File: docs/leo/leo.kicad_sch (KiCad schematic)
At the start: 21 parts, among them IC11 GAL16V8, IC20 74153, IC21 74LS273, IC29 74LS273, IC37 MB81C78A, IC38 MB81C78A, IC40 74LS04, IC41 GAL16V8, IC51 GAL16V8, IC52 74LS32, IC56 74LS245, IC57 74LS245, IC58 74LS244, IC59 74LS244, IC60 74LS244, IC61 74LS139, IC62 74LS20, IC8 7486

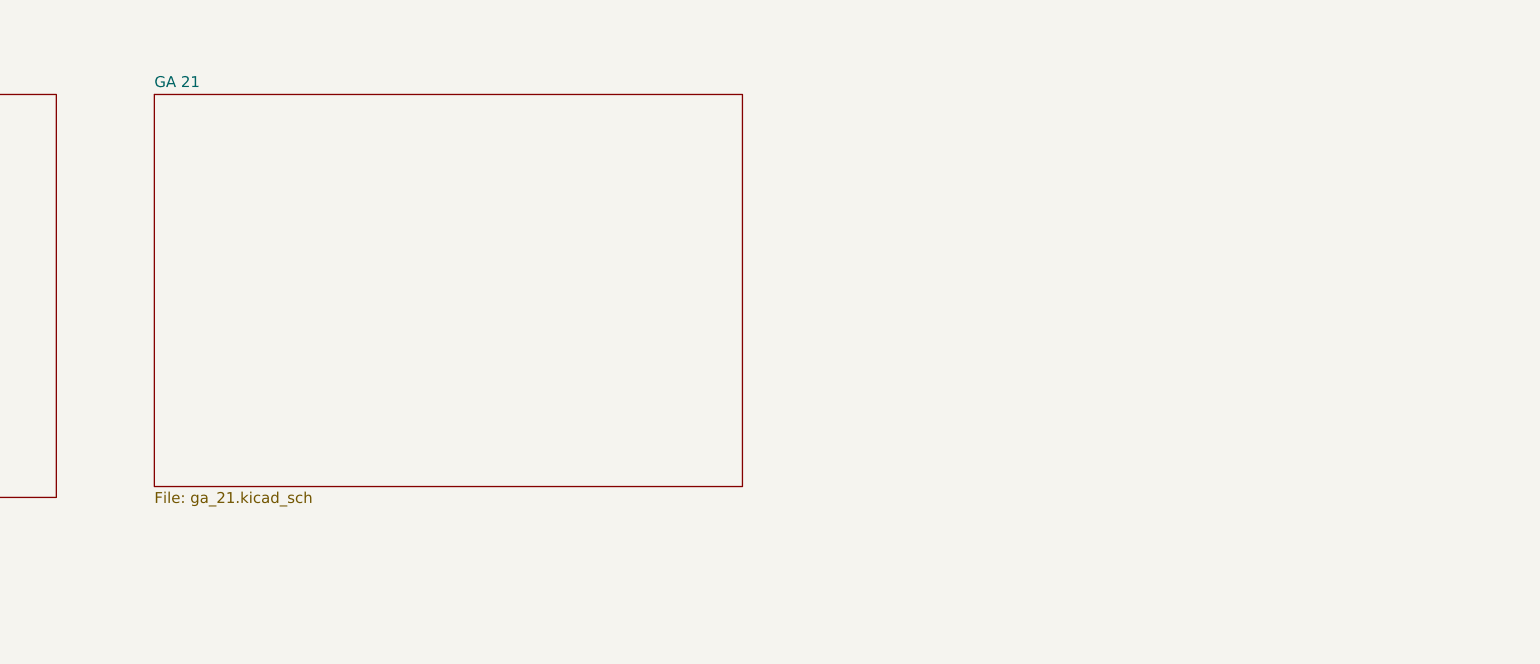
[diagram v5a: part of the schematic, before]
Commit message: Added GA22 symbol
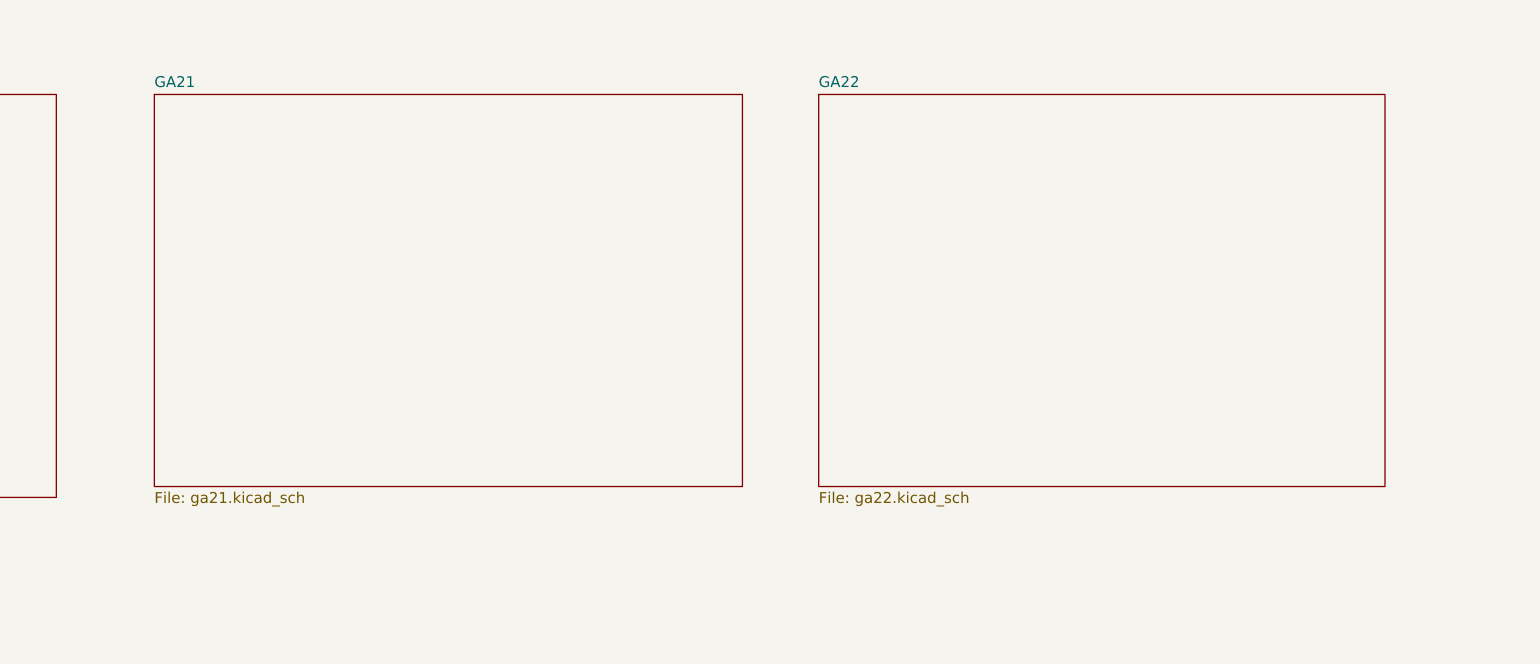
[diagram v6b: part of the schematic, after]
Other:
- sheet GA 21 renamed GA21
- added sheet GA22 (ga22.kicad_sch)
- sheet GA21: file ga_21.kicad_sch -> ga21.kicad_sch
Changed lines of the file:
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@@
     (stroke (width 0.1524) (type solid) (color 0 0 0 0))
     (fill (color 0 0 0 0.0000))
-    (property "Sheet name" "GA 21" (id 0) (at 285.75 41.1984 0)
-      (effects (font (size 1.27 1.27)) (justify left bottom))
-    )
-    (property "Sheet file" "ga_21.kicad_sch" (id 1) (at 285.75 88.2146 0)
+    (property "Sheet name" "GA21" (id 0) (at 285.75 41.1984 0)
+      (effects (font (size 1.27 1.27)) (justify left bottom))
+    )
+    (property "Sheet file" "ga21.kicad_sch" (id 1) (at 285.75 88.2146 0)
       (effects (font (size 1.27 1.27)) (justify left top))
     )
@@
     )
     (property "Sheet file" "palette_ram.kicad_sch" (id 1) (at 55.88 89.4846 0)
+      (effects (font (size 1.27 1.27)) (justify left top))
+    )
+  )
+  (sheet (at 363.22 41.91) (size 66.04 45.72) (fields_autoplaced)
+    (stroke (width 0.1524) (type solid) (color 0 0 0 0))
+    (fill (color 0 0 0 0.0000))
+    (property "Sheet name" "GA22" (id 0) (at 363.22 41.1984 0)
+      (effects (font (size 1.27 1.27)) (justify left bottom))
+    )
+    (property "Sheet file" "ga22.kicad_sch" (id 1) (at 363.22 88.2146 0)
       (effects (font (size 1.27 1.27)) (justify left top))
     )
@@
     (path "/3c8e9905-8b74-4eb3-9c18-3105ee09a33f" (page "4"))
     (path "/0bd61519-701e-4675-a889-b424ac477c32" (page "5"))
+    (path "/c1977d2d-8f37-45fb-befe-52187747618e" (page "6"))
   )
   (symbol_instances
@@
       (reference "IC62") (unit 2) (value "74LS20") (footprint "")
     )
+    (path "/c1977d2d-8f37-45fb-befe-52187747618e/7af1c0a0-2edc-4a0d-88a7-73759f63a8a1"
+      (reference "IC63") (unit 1) (value "GA22") (footprint "")
+    )
     (path "/3c8e9905-8b74-4eb3-9c18-3105ee09a33f/1a77a52a-b972-45fe-b376-224bbc5471ec"

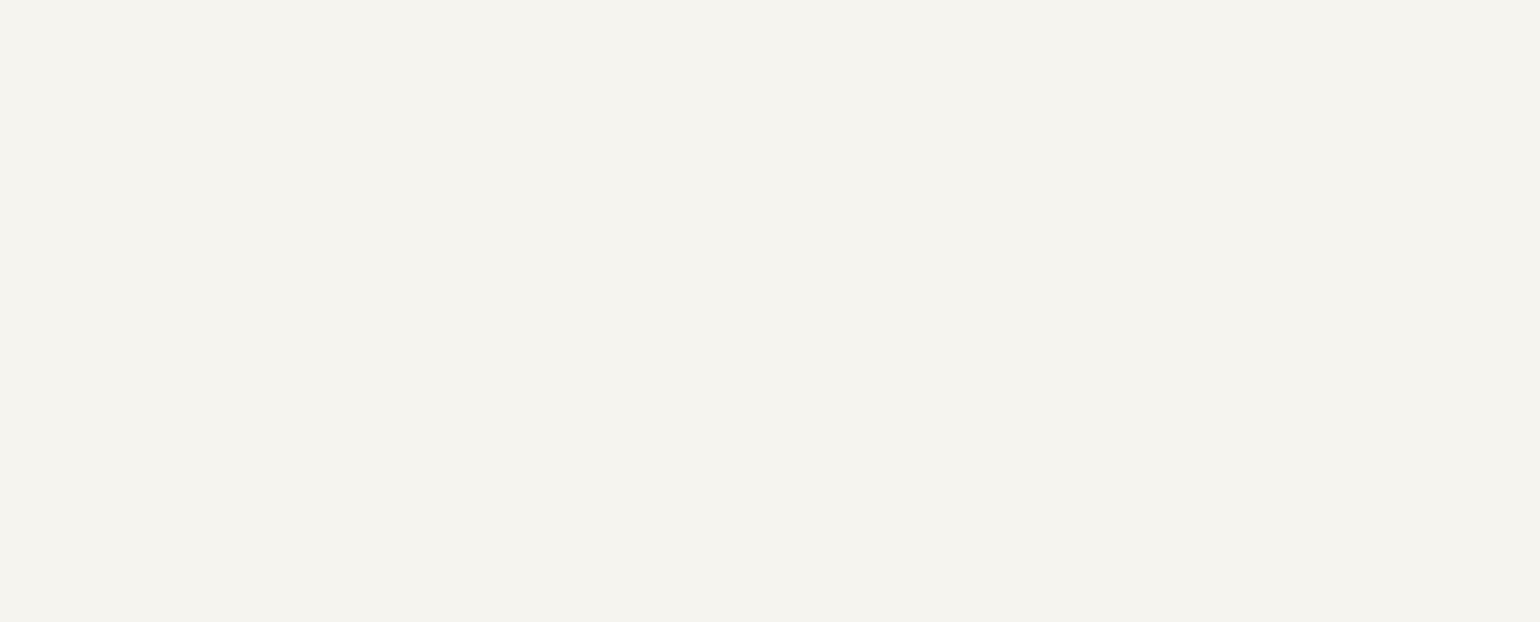
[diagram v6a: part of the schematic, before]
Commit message: Add VRAM and B board interface
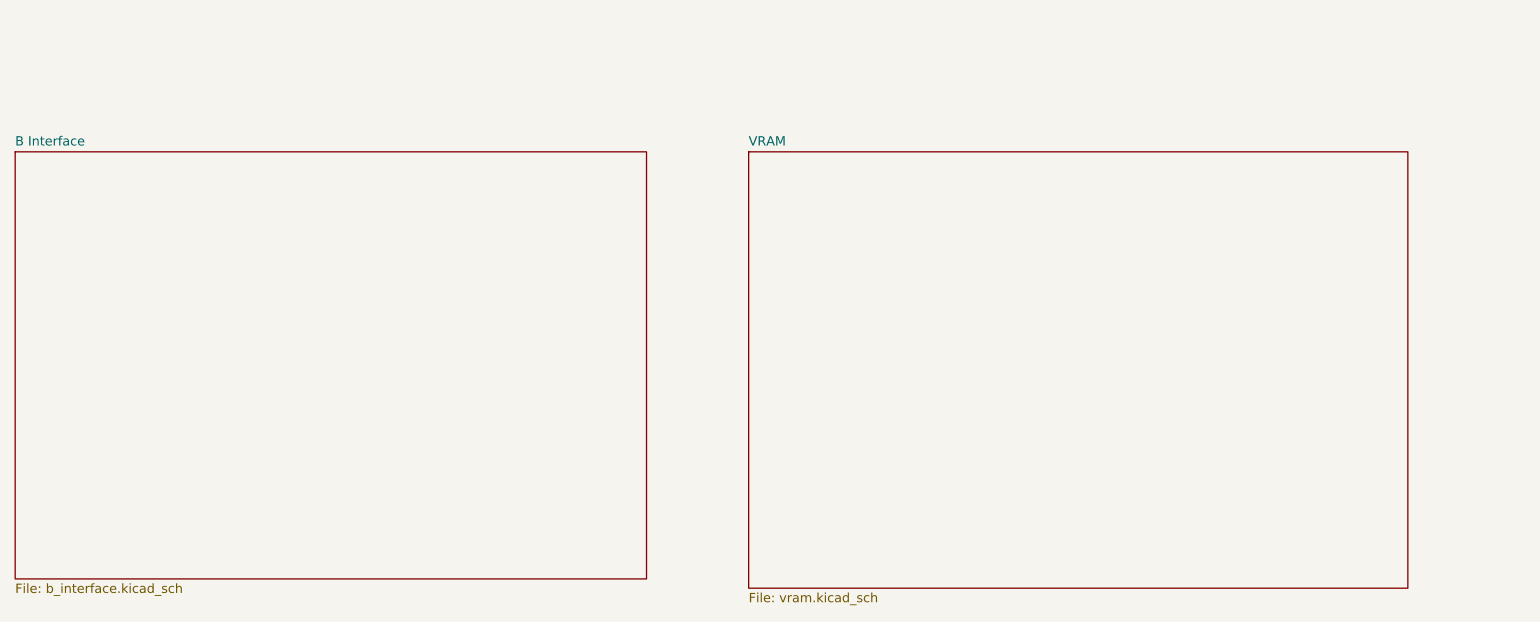
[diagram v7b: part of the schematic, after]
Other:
- added sheet B Interface (b_interface.kicad_sch)
- added sheet VRAM (vram.kicad_sch)
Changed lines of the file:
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@@
+    )
+  )
+  (sheet (at 53.34 728.98) (size 86.36 58.42) (fields_autoplaced)
+    (stroke (width 0.1524) (type solid) (color 0 0 0 0))
+    (fill (color 0 0 0 0.0000))
+    (property "Sheet name" "B Interface" (id 0) (at 53.34 728.2684 0)
+      (effects (font (size 1.27 1.27)) (justify left bottom))
+    )
+    (property "Sheet file" "b_interface.kicad_sch" (id 1) (at 53.34 787.9846 0)
+      (effects (font (size 1.27 1.27)) (justify left top))
     )
   )
@@
     )
     (property "Sheet file" "palette_ram.kicad_sch" (id 1) (at 55.88 89.4846 0)
+      (effects (font (size 1.27 1.27)) (justify left top))
+    )
+  )
+  (sheet (at 153.67 728.98) (size 90.17 59.69) (fields_autoplaced)
+    (stroke (width 0.1524) (type solid) (color 0 0 0 0))
+    (fill (color 0 0 0 0.0000))
+    (property "Sheet name" "VRAM" (id 0) (at 153.67 728.2684 0)
+      (effects (font (size 1.27 1.27)) (justify left bottom))
+    )
+    (property "Sheet file" "vram.kicad_sch" (id 1) (at 153.67 789.2546 0)
       (effects (font (size 1.27 1.27)) (justify left top))
     )
@@
     (path "/0bd61519-701e-4675-a889-b424ac477c32" (page "5"))
     (path "/c1977d2d-8f37-45fb-befe-52187747618e" (page "6"))
+    (path "/0f7b84fe-b888-4f3d-a575-5ad84e7ff4af" (page "7"))
+    (path "/95da80d1-f524-4dae-9bdb-cc834e22a0a6" (page "8"))
   )
   (symbol_instances
@@
       (reference "IC23") (unit 1) (value "74LS245") (footprint "")
     )
+    (path "/95da80d1-f524-4dae-9bdb-cc834e22a0a6/1185a2dc-4144-4173-929c-52e62db8defd"
+      (reference "IC25") (unit 1) (value "UPD43256AC-10L") (footprint "Package_DIP:DIP-28_W15.24mm")
+    )
     (path "/3f170781-d744-477d-adf1-ed36cff99e11/f833f0c3-4fce-4dd4-96ab-bbcda0f1502d"
       (reference "IC25") (unit 1) (value "74153") (footprint "")
     )
+    (path "/95da80d1-f524-4dae-9bdb-cc834e22a0a6/8af29618-263d-45e7-bd96-94facbb1c9d0"
+      (reference "IC26") (unit 1) (value "UPD43256AC-10L") (footprint "Package_DIP:DIP-28_W15.24mm")
+    )
     (path "/3f170781-d744-477d-adf1-ed36cff99e11/bf475103-d728-4ea9-902f-25e477fa41f3"
       (reference "IC26") (unit 1) (value "74153") (footprint "")
@@
       (reference "IC31") (unit 1) (value "74LS374") (footprint "")
     )
+    (path "/0f7b84fe-b888-4f3d-a575-5ad84e7ff4af/538305b1-8ea6-46ec-b47f-6402c327973d"
+      (reference "IC37") (unit 1) (value "74LS245") (footprint "")
+    )
     (path "/543537a5-77fb-40a8-8960-21af55848bb6"
       (reference "IC37") (unit 1) (value "MB81C78A") (footprint "Package_DIP:DIP-28_W15.24mm")
@@
       (reference "IC38") (unit 1) (value "MB81C78A") (footprint "Package_DIP:DIP-28_W15.24mm")
     )
+    (path "/0f7b84fe-b888-4f3d-a575-5ad84e7ff4af/f72d3c1c-bfd6-4c99-8f0a-4247bbba3a83"
+      (reference "IC38") (unit 1) (value "74LS244") (footprint "")
+    )
+    (path "/0f7b84fe-b888-4f3d-a575-5ad84e7ff4af/f9f51c86-e26f-4635-b036-e42dcb471624"
+      (reference "IC39") (unit 1) (value "74LS374") (footprint "")
+    )
+    (path "/0f7b84fe-b888-4f3d-a575-5ad84e7ff4af/75378f28-a645-48c3-b1e7-a067a94de93b"
+      (reference "IC40") (unit 1) (value "74LS245") (footprint "")
+    )
     (path "/aa3a8dc9-cc96-45e0-a99d-26be5c30776b"
       (reference "IC40") (unit 1) (value "74LS04") (footprint "")
@@
       (reference "IC42") (unit 1) (value "GA21") (footprint "")
     )
+    (path "/0f7b84fe-b888-4f3d-a575-5ad84e7ff4af/ffe01a4e-09f3-498e-89f2-93367b330ac7"
+      (reference "IC46") (unit 1) (value "74LS161") (footprint "")
+    )
+    (path "/0f7b84fe-b888-4f3d-a575-5ad84e7ff4af/a437b037-fbfa-4e63-8307-90129b34e9a9"
+      (reference "IC47") (unit 1) (value "GAL16V8") (footprint "")
+    )
+    (path "/0f7b84fe-b888-4f3d-a575-5ad84e7ff4af/e21bd9bf-5a4c-459e-97f8-8b53fe815d4d"
+      (reference "IC48") (unit 1) (value "74LS374") (footprint "")
+    )
+    (path "/0f7b84fe-b888-4f3d-a575-5ad84e7ff4af/7787d4fe-8fb1-4b6b-aa92-6e104aeb2f07"
+      (reference "IC49") (unit 1) (value "74LS244") (footprint "")
+    )
     (path "/433b0e72-de3e-455f-a050-17638acf1723"

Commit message: Add more b board logic
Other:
- added sheet B Board Support (b_board_support.kicad_sch)
- note added: "Disable data bus buffers when reading from RAM (0xeXXXX) and when the PIC is sending vector to CPU."
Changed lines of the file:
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@@
     (stroke (width 0) (type default) (color 0 0 0 0))
+  )
+  (text "Disable data bus buffers when reading from RAM (0xeXXXX)\nand when the PIC is sending vector to CPU."
+    (at 612.14 57.15 0)
+    (effects (font (size 1.27 1.27)) (justify left bottom))
   )
   (label "VID_CTRL13" (at 927.1 246.38 0)
@@
     )
     (property "Sheet file" "b_interface.kicad_sch" (id 1) (at 53.34 787.9846 0)
+      (effects (font (size 1.27 1.27)) (justify left top))
+    )
+  )
+  (sheet (at 266.7 728.98) (size 91.44 60.96) (fields_autoplaced)
+    (stroke (width 0.1524) (type solid) (color 0 0 0 0))
+    (fill (color 0 0 0 0.0000))
+    (property "Sheet name" "B Board Support" (id 0) (at 266.7 728.2684 0)
+      (effects (font (size 1.27 1.27)) (justify left bottom))
+    )
+    (property "Sheet file" "b_board_support.kicad_sch" (id 1) (at 266.7 790.5246 0)
       (effects (font (size 1.27 1.27)) (justify left top))
     )
@@
     (path "/0f7b84fe-b888-4f3d-a575-5ad84e7ff4af" (page "7"))
     (path "/95da80d1-f524-4dae-9bdb-cc834e22a0a6" (page "8"))
+    (path "/179d7767-9223-42a1-9464-f2f519087c7e" (page "9"))
   )
   (symbol_instances
@@
       (reference "#PWR?") (unit 1) (value "VCC") (footprint "")
     )
+    (path "/179d7767-9223-42a1-9464-f2f519087c7e/0a00315c-0294-43da-895d-45ee3e66a96a"
+      (reference "#PWR?") (unit 1) (value "VCC") (footprint "")
+    )
     (path "/0b281849-8f5a-419f-be6f-837b05583d86"
       (reference "#PWR?") (unit 1) (value "GND") (footprint "")
@@
       (reference "#PWR?") (unit 1) (value "VCC") (footprint "")
     )
+    (path "/179d7767-9223-42a1-9464-f2f519087c7e/51e6af43-545a-4ef7-bf04-c381c535fc0b"
+      (reference "#PWR?") (unit 1) (value "VCC") (footprint "")
+    )
     (path "/5497f32e-24b8-48f4-86f2-7b551ebb86e8"
       (reference "#PWR?") (unit 1) (value "GND") (footprint "")
@@
       (reference "#PWR?") (unit 1) (value "GND") (footprint "")
     )
+    (path "/0f7b84fe-b888-4f3d-a575-5ad84e7ff4af/98404a21-fbef-45f4-b16e-531801f9cdd8"
+      (reference "#PWR?") (unit 1) (value "VCC") (footprint "")
+    )
     (path "/9b6f8285-6a81-4874-b589-73198412d6a1"
       (reference "#PWR?") (unit 1) (value "VCC") (footprint "")
@@
       (reference "#PWR?") (unit 1) (value "VCC") (footprint "")
     )
+    (path "/179d7767-9223-42a1-9464-f2f519087c7e/beb61fd4-017a-4806-b8de-53b203a2a546"
+      (reference "#PWR?") (unit 1) (value "VCC") (footprint "")
+    )
     (path "/3f170781-d744-477d-adf1-ed36cff99e11/c7de3329-b4e8-4d45-a030-6104281a2e4a"
       (reference "#PWR?") (unit 1) (value "VCC") (footprint "")
@@
       (reference "#PWR?") (unit 1) (value "GND") (footprint "")
     )
+    (path "/0f7b84fe-b888-4f3d-a575-5ad84e7ff4af/dbec9b6c-9c48-4a59-9a6d-832ed3a15b74"
+      (reference "#PWR?") (unit 1) (value "GND") (footprint "")
+    )
     (path "/e1b825f4-123a-44fe-9974-9687a3e7c3da/e00497ee-2791-45a8-a10c-616edd803b03"
       (reference "#PWR?") (unit 1) (value "GND") (footprint "")
@@
       (reference "IC19") (unit 1) (value "74153") (footprint "")
     )
+    (path "/179d7767-9223-42a1-9464-f2f519087c7e/e957828c-8ddb-47f3-8cca-748e4983cd32"
+      (reference "IC19") (unit 1) (value "74LS175") (footprint "")
+    )
     (path "/defd2b01-d7cf-4e37-9606-5e07d7dff66f"
       (reference "IC20") (unit 1) (value "74153") (footprint "")
     )
+    (path "/179d7767-9223-42a1-9464-f2f519087c7e/fcb0ab9e-f8ad-4a9f-a7fa-1fdd73de4301"
+      (reference "IC20") (unit 1) (value "74LS32") (footprint "")
+    )
+    (path "/179d7767-9223-42a1-9464-f2f519087c7e/cc632f35-a81a-4cd2-a913-c2a169bb1e77"
+      (reference "IC20") (unit 2) (value "74LS32") (footprint "")
+    )
+    (path "/179d7767-9223-42a1-9464-f2f519087c7e/60b0deaa-6516-4777-9a33-22ce9c52c9a8"
+      (reference "IC20") (unit 3) (value "74LS32") (footprint "")
+    )
+    (path "/179d7767-9223-42a1-9464-f2f519087c7e/0ad2f665-99fb-4745-bc47-b38f9457b189"
+      (reference "IC20") (unit 4) (value "74LS32") (footprint "")
+    )
+    (path "/179d7767-9223-42a1-9464-f2f519087c7e/601657c7-5e58-4d08-9d02-ef6301fd4369"
+      (reference "IC20") (unit 5) (value "74LS32") (footprint "")
+    )
+    (path "/179d7767-9223-42a1-9464-f2f519087c7e/ae87740c-a838-441e-941d-a7228e26ab93"
+      (reference "IC21") (unit 1) (value "74LS74") (footprint "")
+    )
     (path "/cf5a2943-a815-42bb-b719-7a470d2cf75b"
       (reference "IC21") (unit 1) (value "74LS273") (footprint "")
     )
+    (path "/179d7767-9223-42a1-9464-f2f519087c7e/602aef1f-1305-4d3a-964b-86853c89a023"
+      (reference "IC21") (unit 2) (value "74LS74") (footprint "")
+    )
+    (path "/179d7767-9223-42a1-9464-f2f519087c7e/93047b01-0304-420d-b1b6-9a2fa4010dd2"
+      (reference "IC21") (unit 3) (value "74LS74") (footprint "")
+    )
+    (path "/179d7767-9223-42a1-9464-f2f519087c7e/0cac01d7-7e3d-4c5f-892b-a55a7ac5dfd0"
+      (reference "IC22") (unit 1) (value "74LS32") (footprint "")
+    )
     (path "/3f170781-d744-477d-adf1-ed36cff99e11/396eddf3-6537-423f-9156-11f40f4239d7"
       (reference "IC22") (unit 1) (value "74LS245") (footprint "")
     )
+    (path "/179d7767-9223-42a1-9464-f2f519087c7e/d2742d46-99b2-41ec-ab29-cfd9f14bc013"
+      (reference "IC22") (unit 2) (value "74LS32") (footprint "")
+    )
+    (path "/179d7767-9223-42a1-9464-f2f519087c7e/ed9bde04-34bb-47da-94c8-079947529e07"
+      (reference "IC22") (unit 3) (value "74LS32") (footprint "")
+    )
+    (path "/179d7767-9223-42a1-9464-f2f519087c7e/48123c14-e992-4e6e-8848-010a46d21281"
+      (reference "IC22") (unit 4) (value "74LS32") (footprint "")
+    )
+    (path "/179d7767-9223-42a1-9464-f2f519087c7e/11099077-7782-4f54-b8a9-5d8f698db765"
+      (reference "IC22") (unit 5) (value "74LS32") (footprint "")
+    )
+    (path "/95da80d1-f524-4dae-9bdb-cc834e22a0a6/5670954d-c5e5-442c-b8a4-2f6fb633eb49"
+      (reference "IC23") (unit 1) (value "74LS273") (footprint "")
+    )
     (path "/3f170781-d744-477d-adf1-ed36cff99e11/67263d0f-a492-4d36-83e2-ce10774430c9"
       (reference "IC23") (unit 1) (value "74LS245") (footprint "")
     )
+    (path "/95da80d1-f524-4dae-9bdb-cc834e22a0a6/f4847a4a-39d4-4089-8027-05d3bc7247e9"
+      (reference "IC24") (unit 1) (value "74LS273") (footprint "")
+    )
     (path "/95da80d1-f524-4dae-9bdb-cc834e22a0a6/1185a2dc-4144-4173-929c-52e62db8defd"
       (reference "IC25") (unit 1) (value "UPD43256AC-10L") (footprint "Package_DIP:DIP-28_W15.24mm")
@@
       (reference "IC28") (unit 1) (value "74153") (footprint "")
     )
+    (path "/179d7767-9223-42a1-9464-f2f519087c7e/80a98361-1417-4d31-b88a-253c2c6fff83"
+      (reference "IC28") (unit 1) (value "74LS138") (footprint "")
+    )
     (path "/3dbda79e-5a9c-4b53-90e5-eb6e514f3b8f"
       (reference "IC29") (unit 1) (value "74LS273") (footprint "")
     )
+    (path "/179d7767-9223-42a1-9464-f2f519087c7e/7004be05-88ae-4977-a9e2-5e69b6d91b34"
+      (reference "IC29") (unit 1) (value "74LS74") (footprint "")
+    )
+    (path "/179d7767-9223-42a1-9464-f2f519087c7e/d25879c3-ae14-43fa-bc44-3c2d5cd89271"
+      (reference "IC29") (unit 2) (value "74LS74") (footprint "")
+    )
+    (path "/179d7767-9223-42a1-9464-f2f519087c7e/739328c2-8fb9-40d3-b978-4f253b191d03"
+      (reference "IC29") (unit 3) (value "74LS74") (footprint "")
+    )
     (path "/3f170781-d744-477d-adf1-ed36cff99e11/df1e08b2-8b8d-453d-ab0a-2d347b006dd1"
       (reference "IC30") (unit 1) (value "74LS374") (footprint "")
@@
       (reference "IC31") (unit 1) (value "74LS374") (footprint "")
     )
+    (path "/179d7767-9223-42a1-9464-f2f519087c7e/4c91eaa6-f6d2-4815-8cde-e92e109c05a9"
+      (reference "IC35") (unit 1) (value "74LS175") (footprint "")
+    )
+    (path "/179d7767-9223-42a1-9464-f2f519087c7e/a7e426fa-892b-4004-b7ff-4f56096c99b6"
+      (reference "IC36") (unit 1) (value "74LS157") (footprint "")
+    )
     (path "/0f7b84fe-b888-4f3d-a575-5ad84e7ff4af/538305b1-8ea6-46ec-b47f-6402c327973d"
       (reference "IC37") (unit 1) (value "74LS245") (footprint "")
@@
       (reference "IC63") (unit 1) (value "GA22") (footprint "")
     )
+    (path "/179d7767-9223-42a1-9464-f2f519087c7e/41f1ebb1-cb26-42fd-97b2-04e392551d7a"
+      (reference "J20") (unit 1) (value "Jumper_3_Bridged12") (footprint "")
+    )
     (path "/3c8e9905-8b74-4eb3-9c18-3105ee09a33f/1a77a52a-b972-45fe-b376-224bbc5471ec"
